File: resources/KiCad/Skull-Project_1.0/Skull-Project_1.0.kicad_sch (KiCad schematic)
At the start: 7 parts, among them SW1 SW_SPST, SW2 SW_SPST

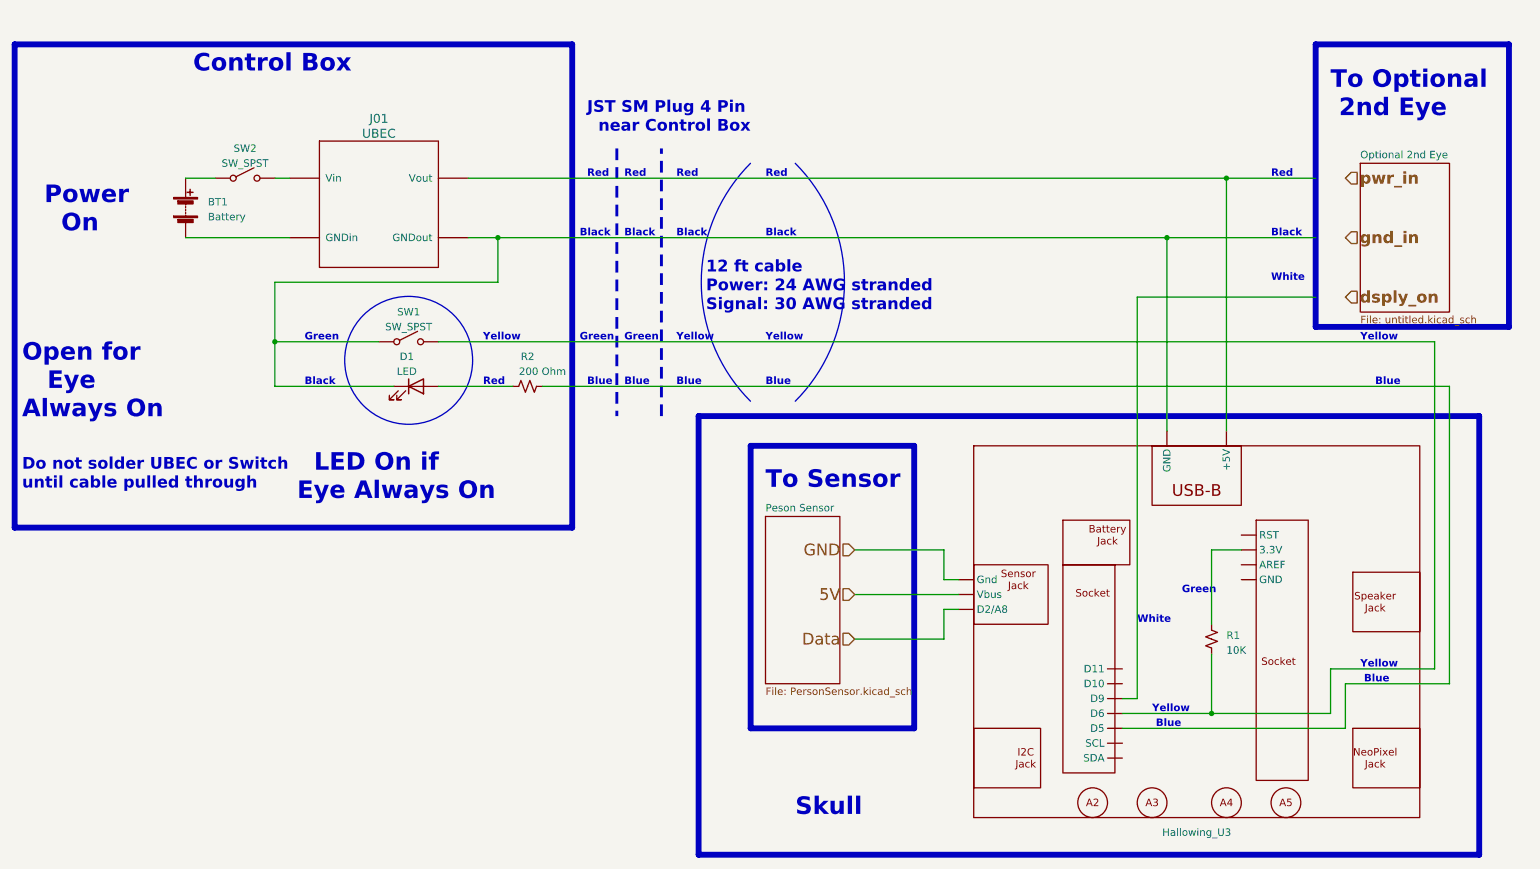
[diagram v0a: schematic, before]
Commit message: microwave sensor now uses NANO for edge detect
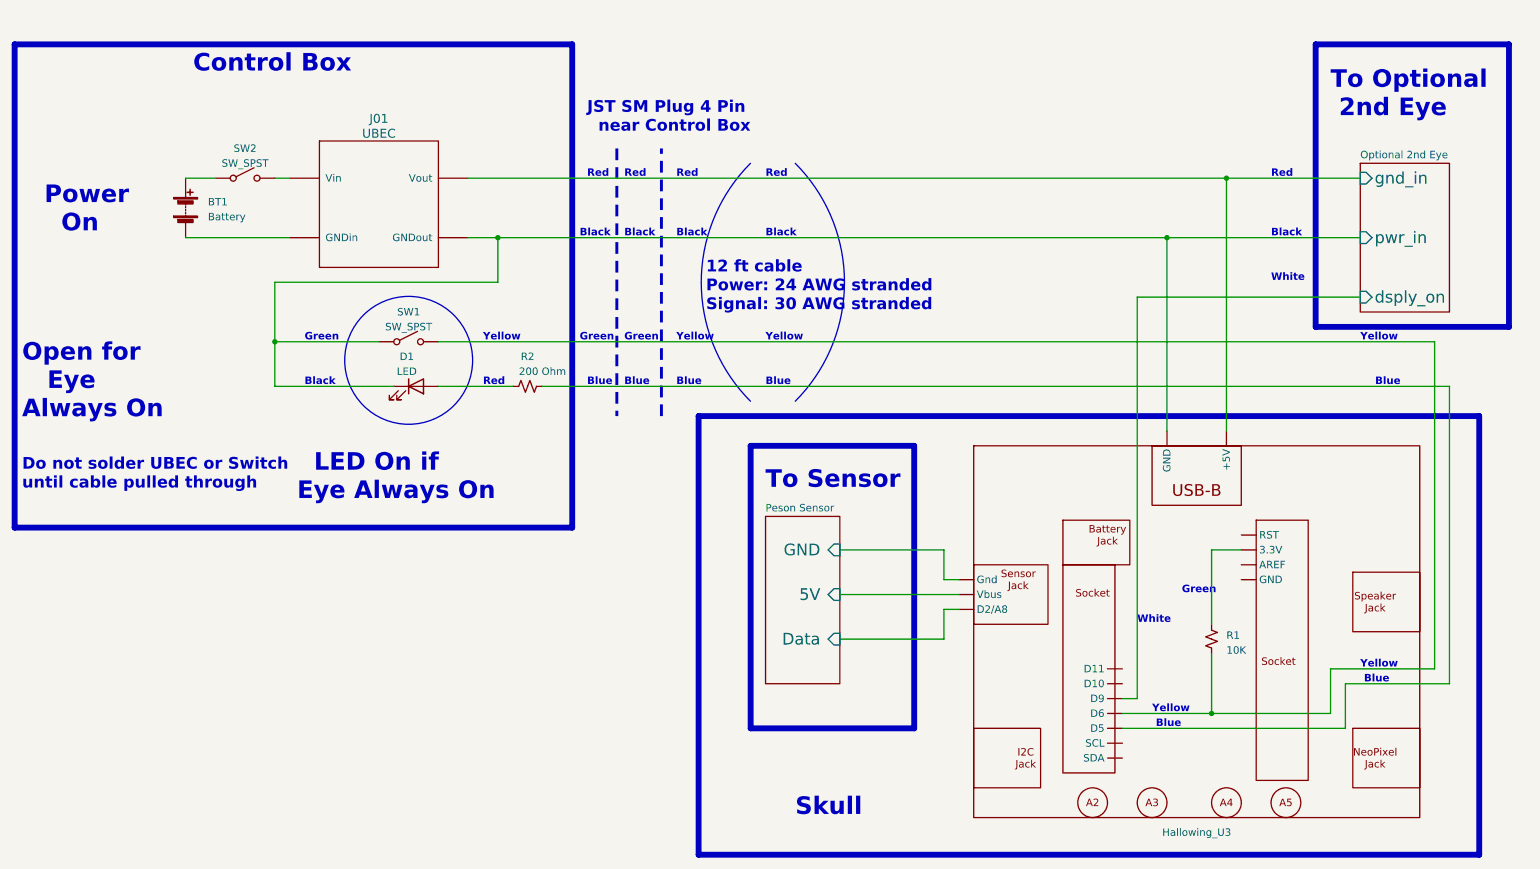
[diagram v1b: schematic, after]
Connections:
- net 5V  is gone; now on net Peson Sensor/GND : Hallowing_U3. (Vbus)
- net Data  is gone; now on net Peson Sensor/GND : Hallowing_U3. (Vbus)
- net GND  is gone; now on net Peson Sensor/GND : Hallowing_U3. (Vbus)
- net at SW2.~ (B): now also BT1.1 (+)
- net Optional 2nd Eye/pwr_in: now reaches D1.1 (K), Hallowing_U3. (Vbus), SW1.~ (B)
- net Peson Sensor/GND : now reaches Hallowing_U3. (Vbus)
- new net: Hallowing_U3. (Vbus), R1.2, SW1.~ (B)
- new net Optional 2nd Eye/dsply_on : Hallowing_U3. (Vbus)
- new net Optional 2nd Eye/gnd_in: Hallowing_U3. (Vbus)
- new net Peson Sensor/5V : Hallowing_U3. (Vbus)
- new net Peson Sensor/Data : Hallowing_U3. (Vbus)
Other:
- sheet Optional 2nd Eye ports: added dsply_on , gnd_in, pwr_in; removed none
- sheet Peson Sensor ports: added 5V , Data , GND ; removed none
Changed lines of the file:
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@@
     (stroke (width 0) (type default))
   )
-  (wire (pts (xy 160.02 111.76) (xy 175.26 111.76))
+  (wire (pts (xy 157.48 111.76) (xy 175.26 111.76))
     (stroke (width 0) (type default))
   )
@@
     (stroke (width 0) (type default))
   )
+  (wire (pts (xy 208.28 68.58) (xy 246.38 68.58))
+    (stroke (width 0) (type default))
+  )
   (wire (pts (xy 261.62 83.82) (xy 261.62 134.62))
     (stroke (width 0) (type default))
@@
     (stroke (width 0) (type default))
   )
-  (wire (pts (xy 160.02 127) (xy 175.26 127))
-    (stroke (width 0) (type default))
-  )
-  (wire (pts (xy 213.36 58.42) (xy 238.76 58.42))
+  (wire (pts (xy 157.48 127) (xy 175.26 127))
     (stroke (width 0) (type default))
   )
@@
     (stroke (width 0) (type default))
   )
-  (wire (pts (xy 223.52 48.26) (xy 238.76 48.26))
+  (wire (pts (xy 213.36 58.42) (xy 246.38 58.42))
+    (stroke (width 0) (type default))
+  )
+  (wire (pts (xy 223.52 48.26) (xy 246.38 48.26))
     (stroke (width 0) (type default))
   )
@@
     (stroke (width 0) (type default))
   )
-  (wire (pts (xy 208.28 68.58) (xy 238.76 68.58))
-    (stroke (width 0) (type default))
-  )
-  (wire (pts (xy 160.02 119.38) (xy 177.8 119.38))
+  (wire (pts (xy 157.48 119.38) (xy 177.8 119.38))
     (stroke (width 0) (type default))
   )
@@
   (text "Blue" (at 211.455 142.24 0)
     (effects (font (size 1.27 1.27) bold) (justify left bottom))
-  )
-  (hierarchical_label "GND " (shape input) (at 160.02 111.76 180) (fields_autoplaced)
-    (effects (font (size 2 2)) (justify right))
-  )
-  (hierarchical_label " pwr_in" (shape input) (at 243.84 48.26 0) (fields_autoplaced)
-    (effects (font (size 2 2) bold) (justify left))
-  )
-  (hierarchical_label "5V " (shape input) (at 160.02 119.38 180) (fields_autoplaced)
-    (effects (font (size 2 2)) (justify right))
-  )
-  (hierarchical_label " dsply_on" (shape input) (at 243.84 68.58 0) (fields_autoplaced)
-    (effects (font (size 2 2) bold) (justify left))
-  )
-  (hierarchical_label "Data " (shape input) (at 160.02 127 180) (fields_autoplaced)
-    (effects (font (size 2 2)) (justify right))
-  )
-  (hierarchical_label " gnd_in" (shape input) (at 243.84 58.42 0) (fields_autoplaced)
-    (effects (font (size 2 2) bold) (justify left))
   )
   (symbol (lib_id "MDO:UBEC") (at 76.2 54.61 0) (unit 1)
@@
     )
     (property "Sheetfile" "untitled.kicad_sch" (at 246.38 71.7046 0)
-      (effects (font (size 1.27 1.27)) (justify left top))
+      (effects (font (size 1.27 1.27)) (justify left top) hide)
+    )
+    (pin "gnd_in" input (at 246.38 48.26 180)
+      (effects (font (size 2 2)) (justify left))
+    )
+    (pin "pwr_in" input (at 246.38 58.42 180)
+      (effects (font (size 2 2)) (justify left))
+    )
+    (pin "dsply_on " input (at 246.38 68.58 180)
+      (effects (font (size 2 2)) (justify left))
     )
     (instances
@@
     )
     (property "Sheetfile" "PersonSensor.kicad_sch" (at 144.78 135.2046 0)
-      (effects (font (size 1.27 1.27)) (justify left top))
+      (effects (font (size 1.27 1.27)) (justify left top) hide)
     )
     (property "Field2" "" (at 144.78 106.045 0)
       (effects (font (size 1.27 1.27)) hide)
     )
-    (instances
+    (pin "GND " input (at 157.48 111.76 0)
+      (effects (font (size 2 2)) (justify right))
+    )
+    (pin "Data " input (at 157.48 127 0)
+      (effects (font (size 2 2)) (justify right))
+    )
+    (pin "5V " input (at 157.48 119.38 0)
+      (effects (font (size 2 2)) (justify right))
+    )
+    (instances

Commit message: schematic update pin on NANO
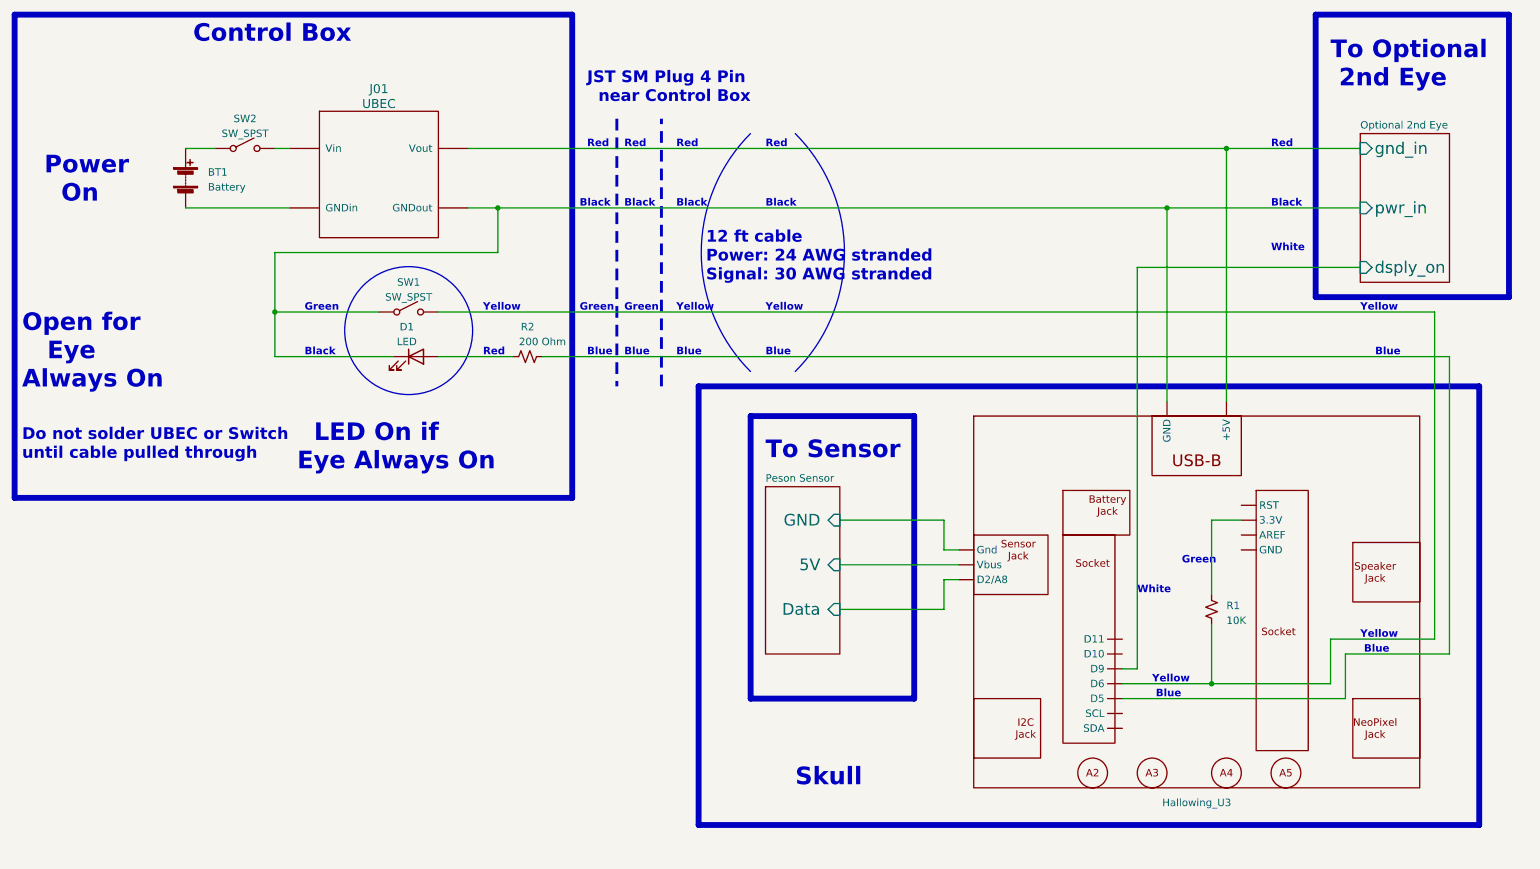
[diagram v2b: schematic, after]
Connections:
- net at SW2.~ (B): now also BT1.1 (+)
- new net: Hallowing_U3. (Vbus), R1.2, SW1.~ (B)
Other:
- moved on the sheet: BT1, D1, Hallowing_U3, R1, R2, SW1, SW2

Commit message: correct schematic 3K/7K resistors
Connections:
- net at SW2.~ (B): now also BT1.1 (+)
- new net: Hallowing_U3. (Vbus), R1.2, SW1.~ (B)

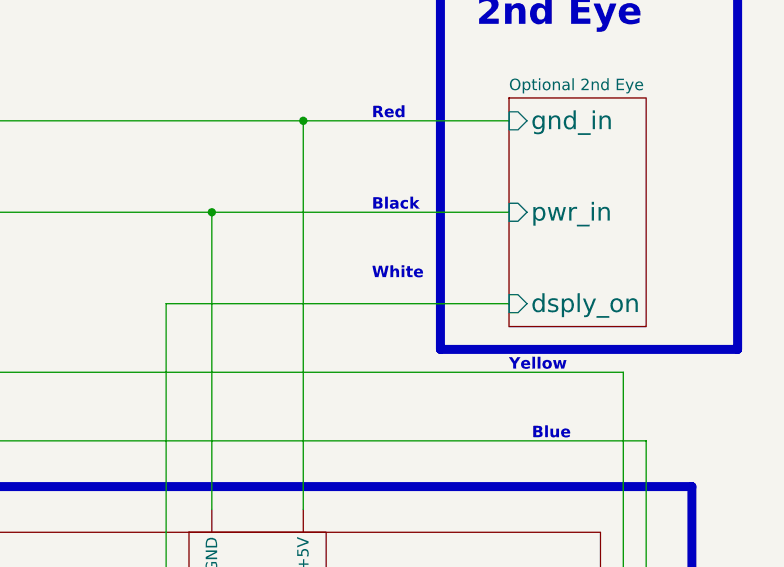
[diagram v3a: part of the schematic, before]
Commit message: add wire colors to schematic
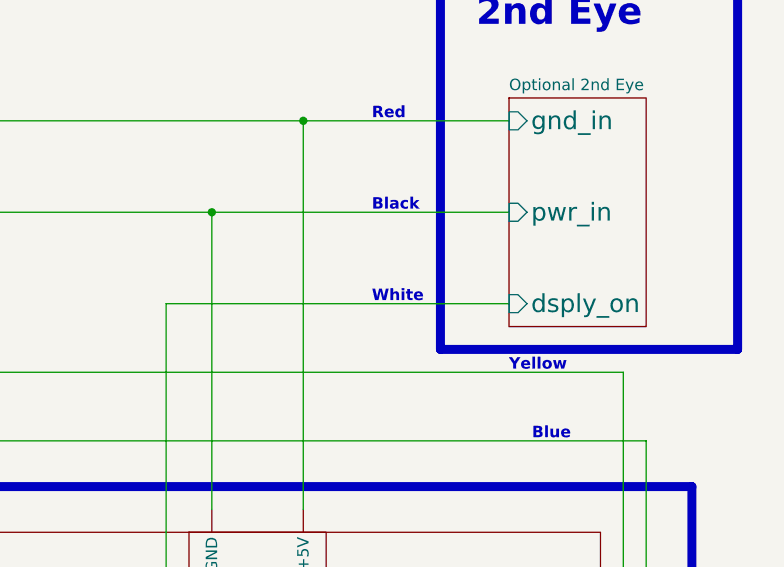
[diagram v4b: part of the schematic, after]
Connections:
- net at SW2.~ (B): now also BT1.1 (+)
- new net: Hallowing_U3. (Vbus), R1.2, SW1.~ (B)
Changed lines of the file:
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@@
   (title_block
     (title "Skull-Project 1.0")
-    (date "2024-09-19")
+    (date "2024-09-20")
     (rev "1.0")
     (company "github.com/Mark-MDO47/Skull-Project")
@@
     (effects (font (size 1.27 1.27) (thickness 0.254) bold) (justify left bottom))
   )
-  (text "White" (at 231.14 60.96 0)
-    (effects (font (size 1.27 1.27) bold) (justify left bottom))
-  )
+  (text "White" (at 231.14 63.5 0)
+    (effects (font (size 1.27 1.27) bold) (justify left bottom))
+  )
